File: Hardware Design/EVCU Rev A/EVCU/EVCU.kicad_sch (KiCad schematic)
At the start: 63 parts, among them J1 Conn_01x06, J2 Conn_01x02, J3 APPS_Conn, J4 Micro_SD_Card, J5 DB9_Male, U1 BD33FC0WEFJ_E2, U10 EMIF06-MSD02N16, U11 ESDALC6V1W5, U2 MC7805CDTRKG, U3 STM32L4R9ZITx, U4 MCP3208, U5 MPU-6500, U6 SN65HVD230, U7 LM358, U8 LM358, U9 ESDCAN24-2BLY, X1 ECS-2520MV-160-CN-TR

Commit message: EVCU BOM
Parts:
- C29: value C_Small -> 0.1uF; footprint (none) -> Capacitor_SMD:C_0603_1608Metric_Pad1.08x0.95mm_HandSolder; Rating (none) -> 10V; Tolerance (none) -> 5%
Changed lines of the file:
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@@
     (pin "1")
-  )
-  (symbol (lib_id "Device:C_Small") (at 477.52 193.04 0) (unit 1)
-    (in_bom yes) (on_board yes) (fields_autoplaced)
-    (property "Reference" "C29" (id 0) (at 479.8441 192.2116 0)
-      (effects (font (size 1.27 1.27)) (justify left))
-    )
-    (property "Value" "C_Small" (id 1) (at 479.8441 194.7485 0)
-      (effects (font (size 1.27 1.27)) (justify left))
-    )
-    (property "Footprint" "" (id 2) (at 477.52 193.04 0)
-      (effects (font (size 1.27 1.27)) hide)
-    )
-    (property "Datasheet" "~" (id 3) (at 477.52 193.04 0)
-      (effects (font (size 1.27 1.27)) hide)
-    )
-    (pin "1")
-    (pin "2")
   )
   (symbol (lib_id "power:GND") (at 454.66 226.06 0) (unit 1)
@@
     )
     (pin "1")
+  )
+  (symbol (lib_id "Device:C_Small") (at 477.52 193.04 0) (mirror y) (unit 1)
+    (in_bom yes) (on_board yes)
+    (property "Reference" "C29" (id 0) (at 475.615 190.6 0)
+      (effects (font (size 1.27 1.27)) (justify left))
+    )
+    (property "Value" "0.1uF" (id 1) (at 475.525 192.532 0)
+      (effects (font (size 1.27 1.27)) (justify left))
+    )
+    (property "Footprint" "Capacitor_SMD:C_0603_1608Metric_Pad1.08x0.95mm_HandSolder" (id 2) (at 477.52 193.04 0)
+      (effects (font (size 1 1)) hide)
+    )
+    (property "Datasheet" "~" (id 3) (at 477.52 193.04 0)
+      (effects (font (size 1 1)) hide)
+    )
+    (property "Rating" "10V" (id 4) (at 475.615 194.31 0)
+      (effects (font (size 1.27 1.27)) (justify left))
+    )
+    (property "Tolerance" "5%" (id 5) (at 475.615 195.961 0)
+      (effects (font (size 1.27 1.27)) (justify left))
+    )
+    (pin "1")
+    (pin "2")
   )
   (symbol (lib_id "Amplifier_Operational:LM358") (at 533.4 147.32 0) (mirror y) (unit 1)
@@
       (reference "C28") (unit 1) (value "0.1uF") (footprint "Capacitor_SMD:C_0603_1608Metric_Pad1.08x0.95mm_HandSolder")
     )
-    (path "/54adadf1-54ce-495b-911f-436f6409b690"
-      (reference "C29") (unit 1) (value "C_Small") (footprint "")
+    (path "/8fd13a7d-1205-476d-b3c7-54da863d0408"
+      (reference "C29") (unit 1) (value "0.1uF") (footprint "Capacitor_SMD:C_0603_1608Metric_Pad1.08x0.95mm_HandSolder")
     )
     (path "/1ebdb596-e85b-47a1-8722-877bf4da7f08"

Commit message: joe mamama
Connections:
- net MISO: no longer J4.7 (DAT0), U10.7 (DAT0_In)
- net MOSI: no longer J4.3 (CMD), U10.5 (CMD_In)
- net SCK: no longer J4.5 (CLK), U10.6 (CLK_In)
- net SD_CS: no longer J4.2 (DAT3/CD), U10.4 (DAT3_In)
- new net FILTER_CS: J4.2 (DAT3/CD), U10.4 (DAT3_In)
- new net FILTER_MISO: J4.7 (DAT0), U10.7 (DAT0_In)
- new net FILTER_MOSI: J4.3 (CMD), U10.5 (CMD_In)
- new net FILTER_SCK: J4.5 (CLK), U10.6 (CLK_In)
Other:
- note removed: "SET GRID TO 2.54mm"
- company: University of Alberta Formula Racing -> ECE 490 Group 1
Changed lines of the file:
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@@
   (title_block
     (title "Electric Vehicle Control Unit")
-    (date "2022-11-18")
+    (date "2022-11-19")
     (rev "A")
-    (company "University of Alberta Formula Racing")
-  )
-  (junction (at 292.1 147.32) (diameter 0) (color 0 0 0 0)
+    (company "ECE 490 Group 1")
   )
   (junction (at 251.46 284.48) (diameter 0) (color 0 0 0 0)
@@
   )
   (junction (at 27.94 22.86) (diameter 0) (color 0 0 0 0)
+  )
+  (junction (at 292.1 144.78) (diameter 0) (color 0 0 0 0)
   )
   (junction (at 38.1 33.02) (diameter 0) (color 0 0 0 0)
@@
     (stroke (width 0) (type default) (color 0 0 0 0))
   )
-  (wire (pts (xy 292.1 147.32) (xy 292.1 149.86))
+  (wire (pts (xy 292.1 144.78) (xy 292.1 149.86))
     (stroke (width 0) (type default) (color 0 0 0 0))
   )
@@
     (stroke (width 0) (type default) (color 0 0 0 0))
   )
-  (wire (pts (xy 279.4 147.32) (xy 279.4 144.78))
-    (stroke (width 0) (type default) (color 0 0 0 0))
-  )
   (wire (pts (xy 515.62 38.1) (xy 515.62 43.18))
     (stroke (width 0) (type default) (color 0 0 0 0))
@@
     (stroke (width 0) (type default) (color 0 0 0 0))
   )
+  (wire (pts (xy 274.32 144.78) (xy 292.1 144.78))
+    (stroke (width 0) (type default) (color 0 0 0 0))
+  )
   (wire (pts (xy 482.6 38.1) (xy 485.14 38.1))
     (stroke (width 0) (type default) (color 0 0 0 0))
@@
     (stroke (width 0) (type default) (color 0 0 0 0))
   )
+  (wire (pts (xy 292.1 144.78) (xy 320.04 144.78))
+    (stroke (width 0) (type default) (color 0 0 0 0))
+  )
   (wire (pts (xy 63.5 124.46) (xy 63.5 127))
     (stroke (width 0) (type default) (color 0 0 0 0))
@@
     (stroke (width 0) (type default) (color 0 0 0 0))
   )
-  (wire (pts (xy 274.32 144.78) (xy 279.4 144.78))
-    (stroke (width 0) (type default) (color 0 0 0 0))
-  )
   (wire (pts (xy 99.06 22.86) (xy 99.06 25.4))
     (stroke (width 0) (type default) (color 0 0 0 0))
@@
     (stroke (width 0) (type default) (color 0 0 0 0))
   )
-  (wire (pts (xy 279.4 147.32) (xy 292.1 147.32))
-    (stroke (width 0) (type default) (color 0 0 0 0))
-  )
   (wire (pts (xy 88.9 33.02) (xy 78.74 33.02))
     (stroke (width 0) (type default) (color 0 0 0 0))
@@
     (stroke (width 0) (type default) (color 0 0 0 0))
   )
-  (wire (pts (xy 292.1 147.32) (xy 325.12 147.32))
+  (wire (pts (xy 320.04 144.78) (xy 320.04 147.32))
     (stroke (width 0) (type default) (color 0 0 0 0))
   )
@@
   )
   (wire (pts (xy 63.5 116.84) (xy 63.5 119.38))
+    (stroke (width 0) (type default) (color 0 0 0 0))
+  )
+  (wire (pts (xy 320.04 147.32) (xy 325.12 147.32))
     (stroke (width 0) (type default) (color 0 0 0 0))
   )
@@
     (effects (font (size 3 3)) (justify left bottom))
   )
-  (text "SET GRID TO 2.54mm\n" (at -17.78 17.78 0)
-    (effects (font (size 40 40)) (justify left bottom))
-  )
   (label "LMBOUT" (at 525.78 134.62 0)
     (effects (font (size 1.27 1.27)) (justify left bottom))
@@
     (effects (font (size 1.27 1.27)) (justify right bottom))
   )
-  (label "SWCLK" (at 279.4 144.78 0)
+  (label "SWCLK" (at 281.94 144.78 0)
     (effects (font (size 1.27 1.27)) (justify left bottom))
   )
@@
     (effects (font (size 1.27 1.27)) (justify left bottom))
   )
-  (label "SD_CS" (at 485.14 208.28 0)
+  (label "FILTER_CS" (at 485.14 208.28 0)
     (effects (font (size 1.27 1.27)) (justify left bottom))
   )
@@
     (effects (font (size 1.27 1.27)) (justify left bottom))
   )
-  (label "SCK" (at 485.14 215.9 0)
+  (label "FILTER_SCK" (at 485.14 215.9 0)
     (effects (font (size 1.27 1.27)) (justify left bottom))
   )
@@
     (effects (font (size 1.27 1.27)) (justify right bottom))
   )
-  (label "MOSI" (at 485.14 210.82 0)
+  (label "FILTER_MOSI" (at 485.14 210.82 0)
     (effects (font (size 1.27 1.27)) (justify left bottom))
   )
@@
     (effects (font (size 1.27 1.27)) (justify left bottom))
   )
-  (label "MISO" (at 485.14 220.98 0)
-    (effects (font (size 1.27 1.27)) (justify left bottom))
-  )
+  (label "FILTER_MISO" (at 485.14 220.98 0)
+    (effects (font (size 1.27 1.27)) (justify left bottom))
+  )

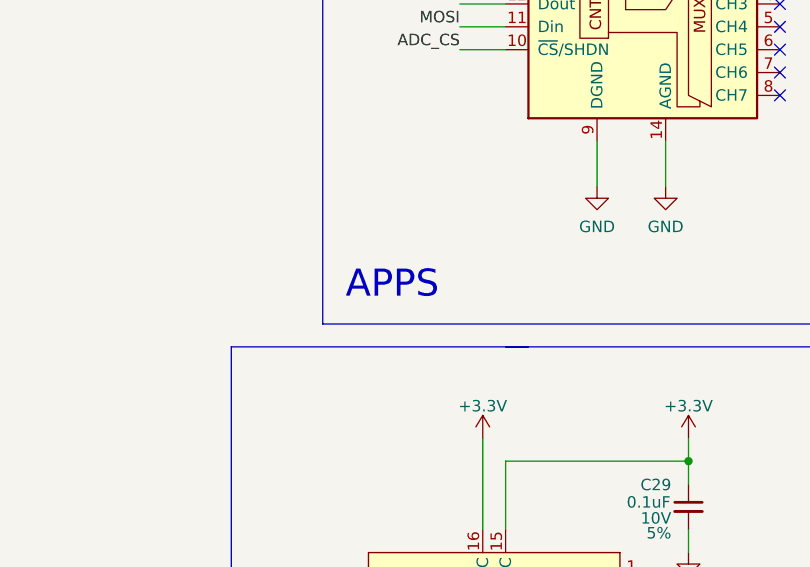
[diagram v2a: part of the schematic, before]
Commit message: what
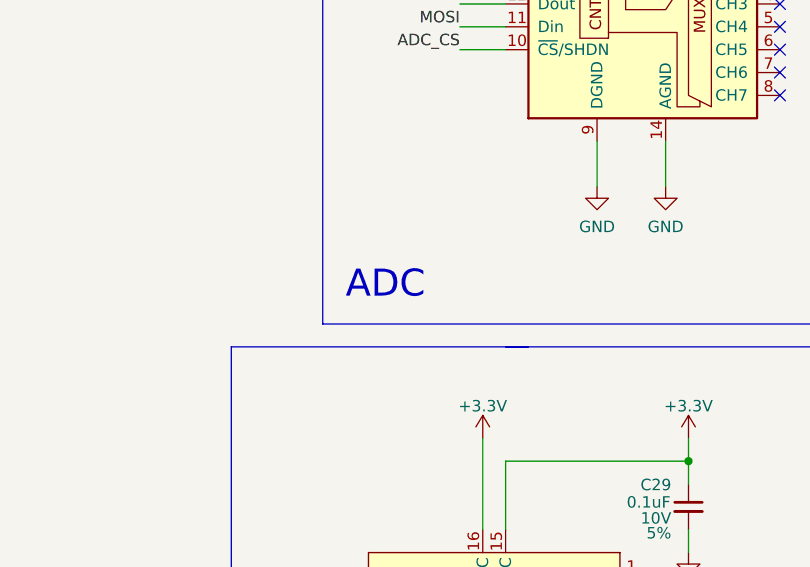
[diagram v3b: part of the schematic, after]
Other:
- note added: "ADC"
- note removed: "APPS"
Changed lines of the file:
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@@
     (effects (font (size 3 3)) (justify left bottom))
   )
-  (text "APPS\n" (at 439.42 170.18 0)
+  (text "ADC" (at 439.42 170.18 0)
     (effects (font (size 3 3)) (justify left bottom))
   )
@@
     (pin "2")
     (pin "3")
-    (pin "5")
-    (pin "6")
-    (pin "7")
-    (pin "4")
-    (pin "8")
   )
   (symbol (lib_id "power:GND") (at 513.08 124.46 0) (unit 1)
@@
     (pin "2")
     (pin "3")
-    (pin "5")
-    (pin "6")
-    (pin "7")
-    (pin "4")
-    (pin "8")
   )
   (symbol (lib_id "Connector_Generic:Conn_01x02") (at 93.98 96.52 0) (unit 1)
@@
       (effects (font (size 1.27 1.27)) hide)
     )
-    (pin "1")
-    (pin "2")
-    (pin "3")
-    (pin "5")
-    (pin "6")
-    (pin "7")
     (pin "4")
     (pin "8")

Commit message: .
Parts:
- removed C22: 10uF, Capacitor_SMD:C_0603_1608Metric_Pad1.08x0.95mm_HandSolder, symbol Device:C_Small
- removed C23: 1uF, Capacitor_SMD:C_0603_1608Metric_Pad1.08x0.95mm_HandSolder, symbol Device:C_Small
- removed U2: MC7805CDTRKG, Package_TO_SOT_SMD:TO-252-2, symbol Regulator_Linear:MC7805CDTRKG
- removed U4: MCP3208, symbol Analog_ADC:MCP3208
- added U?: AP62250Z6, Package_TO_SOT_SMD:SOT-563, symbol Regulator_Switching:AP62250Z6
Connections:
- net +3.3VA: no longer U3.29 (VREF+)
- net +3V3: now also C29.2; no longer C29.1
- net FILTER_CS: now also U10.13 (DAT3_EX); no longer U10.4 (DAT3_In)
- net GND: now also C29.1, U?.3 (GND); no longer C29.2
- net MISO: now also U10.7 (DAT0_In); no longer U10.10 (DAT0_Ex)
- net MOSI: now also U10.5 (CMD_In); no longer U10.12 (CMD_Ex)
- net SCK: now also U10.6 (CLK_In); no longer U10.11 (CLK_Ex)
- net SD_CS: now also U10.4 (DAT3_In); no longer U10.13 (DAT3_EX)
- net VOUT_1_APPS: now also U3.71 (PB14)
- net VOUT_2_APPS: now also U3.72 (PB15)
- net at J4.1 (DAT2): now also U10.14 (DAT2_Ex)
- net FILTER_DAT1: now reaches J4.8 (DAT1)
- net FILTER_DAT1: now also U10.9 (DAT1_Ex)
- net FILTER_MISO renamed FILTER_DAT0
- net FILTER_DAT0: now also U10.10 (DAT0_Ex); no longer U10.7 (DAT0_In)
- net FILTER_MOSI renamed FILTER_CMD
- net FILTER_CMD: now also U10.12 (CMD_Ex); no longer U10.5 (CMD_In)
- net FILTER_SCK renamed FILTER_CLK
- net FILTER_CLK: now also U10.11 (CLK_Ex); no longer U10.6 (CLK_In)
- no-connect marks 127 -> 115

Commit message: finishing schematic
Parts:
- removed U?: AP62250Z6, Package_TO_SOT_SMD:SOT-563, symbol Regulator_Switching:AP62250Z6
- added C22: 100nF, Capacitor_SMD:C_0603_1608Metric_Pad1.08x0.95mm_HandSolder, symbol Device:C_Small
- added C23: 22uF, Capacitor_SMD:C_0603_1608Metric_Pad1.08x0.95mm_HandSolder, symbol Device:C_Small
- added J6: Conn_01x02, symbol Connector_Generic:Conn_01x02
- added L2: 2.2uH, symbol Device:L_Small
- added R2: 52.3kR, symbol Device:R_Small
- added R3: 10kR, symbol Device:R_Small
- added U2: AP62250WU-7, Package_TO_SOT_SMD:TSOT-23-6_HandSoldering, symbol Regulator_Switching:AP62250WU-7
- C13: value 0.33uF -> 22uF
- C14: value 100nF -> 2.2uF
- C3: value 0.33uF -> 10uF; Rating 10V -> 20V
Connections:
- net +3.3VA: now also U3.29 (VREF+)
- net +5V: now also C2.1, U1.5 (EN), U1.8 (VCC), C23.1, L2.2, R2.1
- net +BATT: now also U2.3 (VIN); no longer C2.1, U1.5 (EN), U1.8 (VCC)
- net ACCEL_CS: now also U3.69 (PB12); no longer U3.99 (PC7)
- net CAN_H: now also J6.1 (Pin_1); no longer R19.1
- net GND: now also C23.2, R3.2, U2.1 (GND); no longer J1.6 (Pin_6)
- net INT: now also U3.66 (PB11); no longer U3.98 (PC6)
- net MISO: now also U3.71 (PB14); no longer U10.7 (DAT0_In), U3.114 (PC11)
- net MOSI: now also U3.72 (PB15); no longer U10.5 (CMD_In), U3.115 (PC12)
- net SCK: now also U3.70 (PB13); no longer U10.6 (CLK_In), U3.113 (PC10)
- net VOUT_1_APPS: now also U3.31 (PA0); no longer U3.71 (PB14)
- net VOUT_2_APPS: now also U3.32 (PA1); no longer U3.72 (PB15)
- net FILTER_DAT2: now reaches J4.1 (DAT2), U10.14 (DAT2_Ex)
- net MCU_CD: now reaches U10.1 (WP/CD)
- net MCU_CD: now also U3.99 (PC7)
- net MCU_DAT2: now reaches U10.3 (DAT2_In)
- net MCU_DAT2: now also U3.113 (PC10)
- net MCU_DAT1: now reaches U10.8 (DAT1_In)
- net MCU_DAT1: now also U3.101 (PC9)
- net NRST: now reaches C21.1, U3.23 (NRST)
- net NRST: now also J1.6 (Pin_6)
- net MCU_CMD: now reaches U3.118 (PD2)
- net MCU_CMD: now also U10.5 (CMD_In)
- net ADC_CS renamed MCU_DAT0
- net MCU_DAT0: now also U10.7 (DAT0_In)
- net FILTER_CS renamed FILTER_DAT3
- net SD_CS renamed MCU_DAT3
- net MCU_DAT3: now also U3.114 (PC11); no longer U3.101 (PC9)
- new net: R2.2, R3.1, U2.4 (FB)
- new net: J6.2 (Pin_2), R19.1
- new net: C22.2, L2.1, U2.2 (SW)
- new net: C22.1, U2.6 (BST)
- new net MCU_CLK: U10.6 (CLK_In), U3.115 (PC12)
- no-connect marks 115 -> 108
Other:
- moved on the sheet: C13, C3, R19, U9

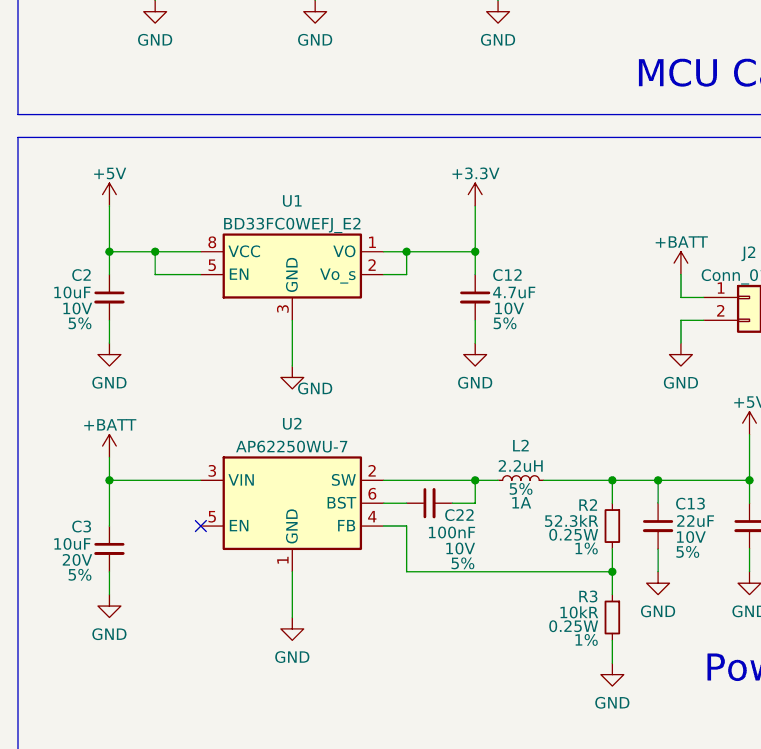
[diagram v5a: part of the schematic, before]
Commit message: SCHEMATIC finish, connector footprint remaining
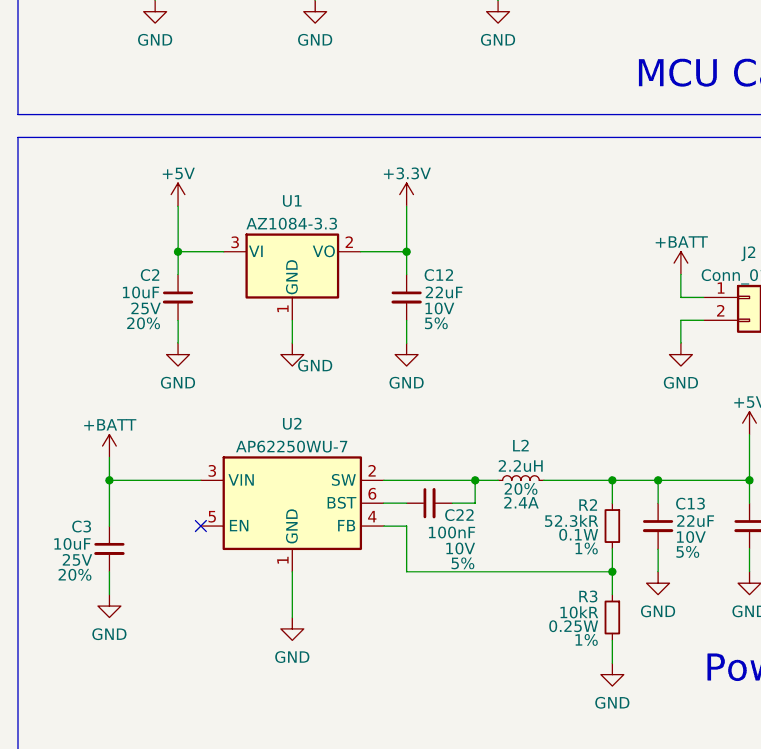
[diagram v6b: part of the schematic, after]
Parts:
- removed U1: BD33FC0WEFJ_E2, Package_SO:HTSOP-8-1EP_3.9x4.9mm_P1.27mm_EP2.4x3.2mm, symbol Regulator_Linear:BD33FC0WEFJ_E2
- added U1: AZ1084-3.3, Package_TO_SOT_SMD:TO-252-3_TabPin2, symbol Regulator_Linear:AZ1084-3.3
- C1, C8: footprint (none) -> Capacitor_SMD:C_0603_1608Metric_Pad1.08x0.95mm_HandSolder
- C12: value 4.7uF -> 22uF; footprint (none) -> Capacitor_SMD:C_0603_1608Metric_Pad1.08x0.95mm_HandSolder
- C2: Rating 10V -> 25V; Tolerance 5% -> 20%
- C3: Rating 20V -> 25V; Tolerance 5% -> 20%
- J1: footprint (none) -> Connector_PinHeader_2.54mm:PinHeader_1x06_P2.54mm_Vertical
- L1: footprint (none) -> Inductor_SMD:L_1210_3225Metric_Pad1.42x2.65mm_HandSolder
- L2: footprint (none) -> Inductor_SMD:L_1008_2520Metric_Pad1.43x2.20mm_HandSolder; Rating 1A -> 2.4A; Tolerance 5% -> 20%
- R1, R10, R11, R12, R13, R14, R15, R16, R17, R18, R19, R3, R6, R7, R8, R9: footprint (none) -> Resistor_SMD:R_0805_2012Metric_Pad1.20x1.40mm_HandSolder
- R2: footprint (none) -> Inductor_SMD:L_0805_2012Metric_Pad1.05x1.20mm_HandSolder; Rating 0.25W -> 0.1W
- U5: footprint QFN24_3X3X0P9_IVS -> Package_DFN_QFN:QFN-24-1EP_3x3mm_P0.4mm_EP1.75x1.6mm_ThermalVias
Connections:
- net +3V3: now also U1.2 (VO)
- net +5V: now also U1.3 (VI)
- net GND: now also U1.1 (GND)

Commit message: Not done some BSE connections and some footprints
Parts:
- added C?: 0.1uF, Capacitor_SMD:C_0603_1608Metric_Pad1.08x0.95mm_HandSolder, symbol Device:C_Small
- added F1: Fuse, symbol Device:Fuse
- added J10, J8, J9, J?: Conn_01x10_Female, Connector_PinSocket_2.54mm:PinSocket_1x10_P2.54mm_Vertical, symbol Connector:Conn_01x10_Female
- added R?: 34kR, Resistor_SMD:R_0805_2012Metric_Pad1.20x1.40mm_HandSolder, symbol Device:R_Small
- added R?: 33kR, Resistor_SMD:R_0805_2012Metric_Pad1.20x1.40mm_HandSolder, symbol Device:R_Small
- added R? (x3): 100kR, Resistor_SMD:R_0805_2012Metric_Pad1.20x1.40mm_HandSolder, symbol Device:R_Small
- added U? (x2): LM358, symbol Amplifier_Operational:LM358
- J3: value APPS_Conn -> APPS/BSE_Conn
- J5: footprint (none) -> Connector_Dsub:DSUB-9_Male_Horizontal_P2.77x2.84mm_EdgePinOffset7.70mm_Housed_MountingHolesOffset9.12mm
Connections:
- net +3V3: now also U?.8 (V+)
- net +5V: now also J3.2 (Pin_2)
- net +BATT: now also F1.1; no longer J2.1 (Pin_1)
- net GND: now also J3.5 (Pin_5), C?.2, R?.2, R?.2, U?.4 (V-)
- net VPA_2: now also J3.4 (Pin_4); no longer J3.3 (Pin_3)
- net VPA_BSE: now reaches J3.1 (Pin_1)
- net VPA_BSE: now also R?.2
- new net: F1.2, J2.1 (Pin_1)
- new net LMA+_BSE: R?.1, R?.2, U?.3 (+)
- new net LMA-_BSE: R?.1, R?.1, U?.2 (-)
- new net LMAOUT_BSE: R?.1, R?.2, U?.1
- new net VOUT_BSE: C?.1, R?.1
- no-connect marks 108 -> 105
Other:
- note added: "ADD BSE INPUT INTO ADC"
- note added: "APPS"
- note added: "BSE"
- note added: "Debug Pins"
- note added: "Not sure if this configuration is right, please double check"
- note removed: "ADC"
- moved on the sheet: C20, C21, C24, C27, C28, C29, D1, J1, J4, R1, U10, U11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

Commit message: basically done, start layout
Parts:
- F1: footprint (none) -> Fuse:Fuse_0805_2012Metric_Pad1.15x1.40mm_HandSolder
- J2, J6: footprint (none) -> TerminalBlock_Phoenix:TerminalBlock_Phoenix_PT-1,5-2-3.5-H_1x02_P3.50mm_Horizontal
- J3: footprint (none) -> Connector_PinSocket_2.54mm:PinSocket_1x06_P2.54mm_Vertical
- gave numbers to parts that had none: 8
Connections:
- net CAN_H: now also J6.2 (Pin_2); no longer J6.1 (Pin_1)
- net VOUT_BSE: now also U3.33 (PA2)
- net at J8.10 (Pin_10): now also J10.1 (Pin_1)
- net at J8.9 (Pin_9): now also J10.2 (Pin_2)
- net at R19.1: now also J6.1 (Pin_1); no longer J6.2 (Pin_2)
- no-connect marks 105 -> 104
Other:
- note added: "Debug Pins (NEED TO BE FIGURED OUT)"
- note removed: "ADD BSE INPUT INTO ADC"
- note removed: "Debug Pins"
- moved on the sheet: J10, J8
